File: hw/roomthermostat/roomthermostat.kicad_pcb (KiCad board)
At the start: 2 copper layers, 68 x 68 mm, 15 parts, among them U1 TSIC206_SOIC8

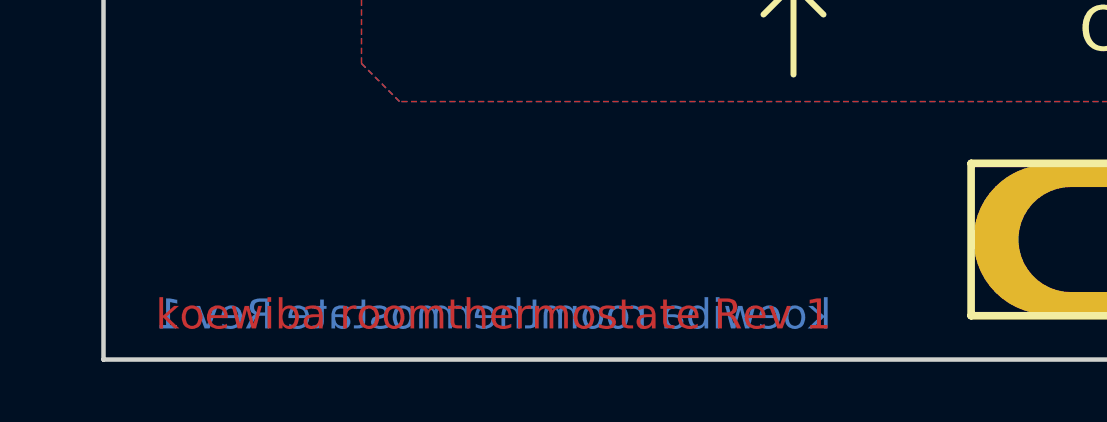
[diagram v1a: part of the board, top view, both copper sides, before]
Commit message: make roomthermostat compatible to bus-module_atmega328 rev A and rev B
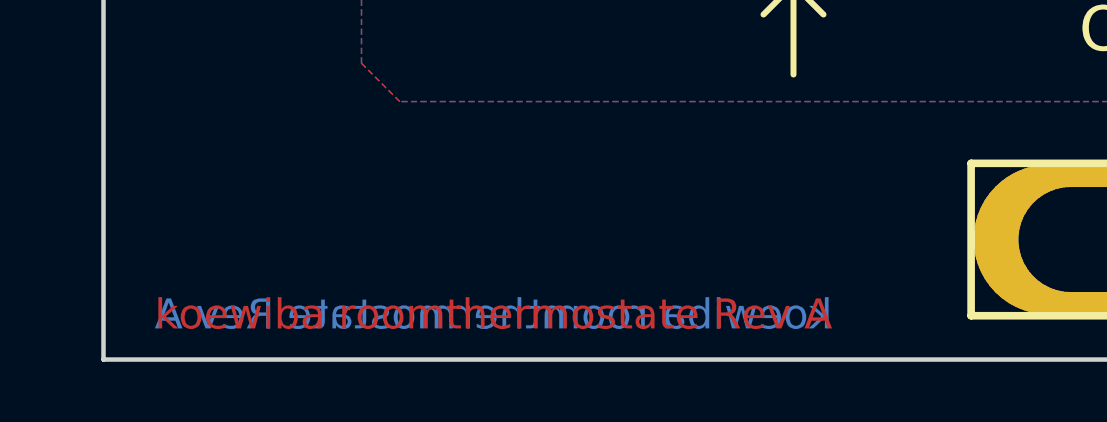
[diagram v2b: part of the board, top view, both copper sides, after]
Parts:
- LOGO1: value Open Hardware -> OPEN_HARDWARE_1
- MOD1: value bus-module_atmega328 -> bus-module_atmega328_revB
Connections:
- MOD1 pad 3: VCC -> (no net)
- MOD1 pad 4: VCC -> (no net)
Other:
- board text added: "koewiba roomthermostate Rev A"
- board text removed: "koewiba roomthermostate Rev 1"
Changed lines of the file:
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@@
   (title_block
     (title roomthermostat)
-    (date 2018-06-14)
-    (rev 1)
+    (date 2018-09-22)
+    (rev A)
     (company koewiba)
   )
@@
       (drillshape 0)
       (scaleselection 1)
-      (outputdirectory "pcb"))
+      (outputdirectory "gerber"))
   )
   (net 0 "")
@@
       (effects (font (size 1 1) (thickness 0.15)) (justify mirror))
     )
-    (fp_text value bus-module_atmega328 (at -12.4 -11.84 90) (layer B.Fab)
+    (fp_text value bus-module_atmega328_revB (at -12.4 -11.84 90) (layer B.Fab)
       (effects (font (size 1 1) (thickness 0.15)) (justify mirror))
     )
@@
     (pad 5 thru_hole circle (at -5.08 0 90) (size 1.8 1.8) (drill 0.9) (layers *.Cu *.Mask B.SilkS)
       (net 11 /KEY1))
-    (pad 4 thru_hole circle (at -2.57 2.54 90) (size 1.8 1.8) (drill 0.9) (layers *.Cu *.Mask B.SilkS)
-      (net 1 VCC))
-    (pad 3 thru_hole circle (at -2.54 0 90) (size 1.8 1.8) (drill 0.9) (layers *.Cu *.Mask B.SilkS)
-      (net 1 VCC))
+    (pad 4 thru_hole circle (at -2.57 2.54 90) (size 1.8 1.8) (drill 0.9) (layers *.Cu *.Mask B.SilkS))
+    (pad 3 thru_hole circle (at -2.54 0 90) (size 1.8 1.8) (drill 0.9) (layers *.Cu *.Mask B.SilkS))
     (pad 2 thru_hole circle (at -0.03 2.54 90) (size 1.8 1.8) (drill 0.9) (layers *.Cu *.Mask B.SilkS)
       (net 2 GND))
@@
       (effects (font (size 1.27 1.27) (thickness 0.254)))
     )
-    (fp_text value "Open Hardware" (at 0.30988 6.56082) (layer F.Fab) hide
+    (fp_text value OPEN_HARDWARE_1 (at 0.30988 6.56082) (layer F.Fab) hide
       (effects (font (size 1.27 1.27) (thickness 0.254)))
     )
@@
     (effects (font (size 1 1) (thickness 0.2)) (justify mirror))
   )
-  (gr_text "koewiba roomthermostate Rev 1" (at 75.915 132.87) (layer B.Cu)
+  (gr_text "koewiba roomthermostate Rev A" (at 75.915 132.87) (layer B.Cu)
     (effects (font (size 1 1) (thickness 0.2)) (justify mirror))
   )
-  (gr_text "koewiba roomthermostate Rev 1" (at 75.915 132.87) (layer F.Cu)
+  (gr_text "koewiba roomthermostate Rev A" (at 75.915 132.87) (layer F.Cu)
     (effects (font (size 1 1) (thickness 0.2)))
   )

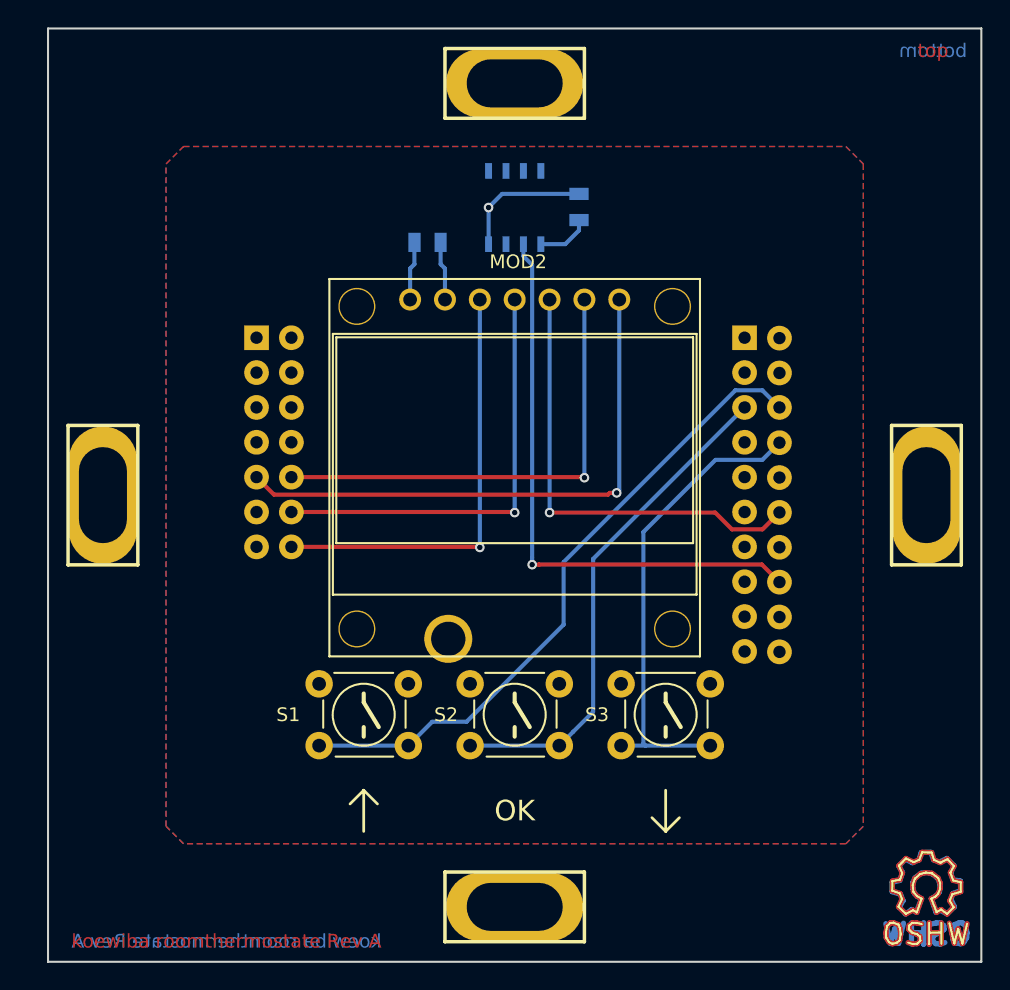
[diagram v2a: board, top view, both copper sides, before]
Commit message: changed pushbuttons of roomthermostate
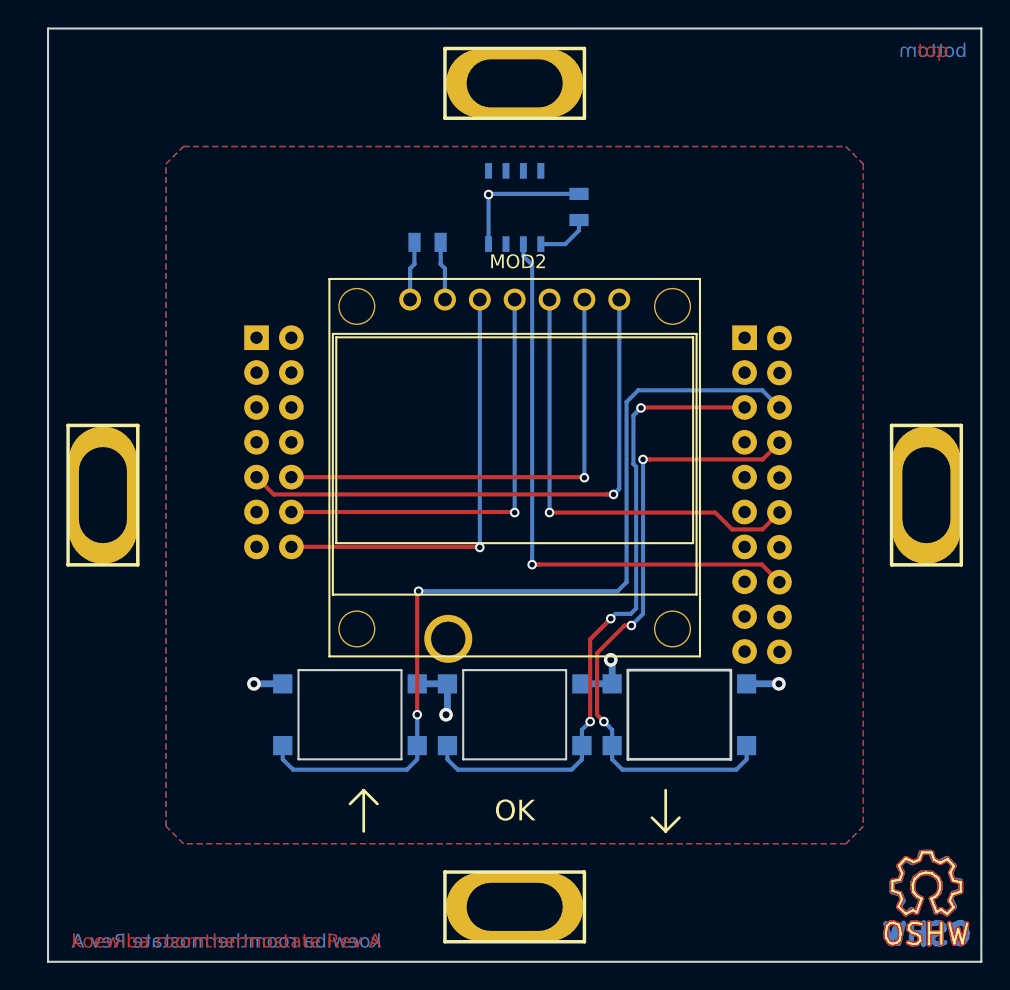
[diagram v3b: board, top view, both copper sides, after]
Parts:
- S1, S2, S3: footprint Switch_Miscelleaneus:PHAP3301 -> Switch_Miscelleaneus:TactileSwitch_SPST_SMD_JTP-1138_BacksideMount; moved to B.Cu
- moved S1 1.00 mm to (84.9, 116.4)
- moved S3 1.00 mm to (108.9, 116.4)
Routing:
- net /KEY0: track 47.5 -> 64.3 mm, vias 0 -> 2
- net GND: track 14.0 -> 27.4 mm, vias 1 -> 5
- net /KEY2: track 34.7 -> 45.8 mm, vias 0 -> 3
- net /KEY1: track 36.7 -> 47.2 mm, vias 0 -> 3
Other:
- outline, holes or cut-outs redrawn
- net class Power added: clearance 0.2, trace_width 0.5, via_dia 1, via_drill 0.5

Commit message: Change pin-assignment of display and temp.sensor
* bumped revision to rev B
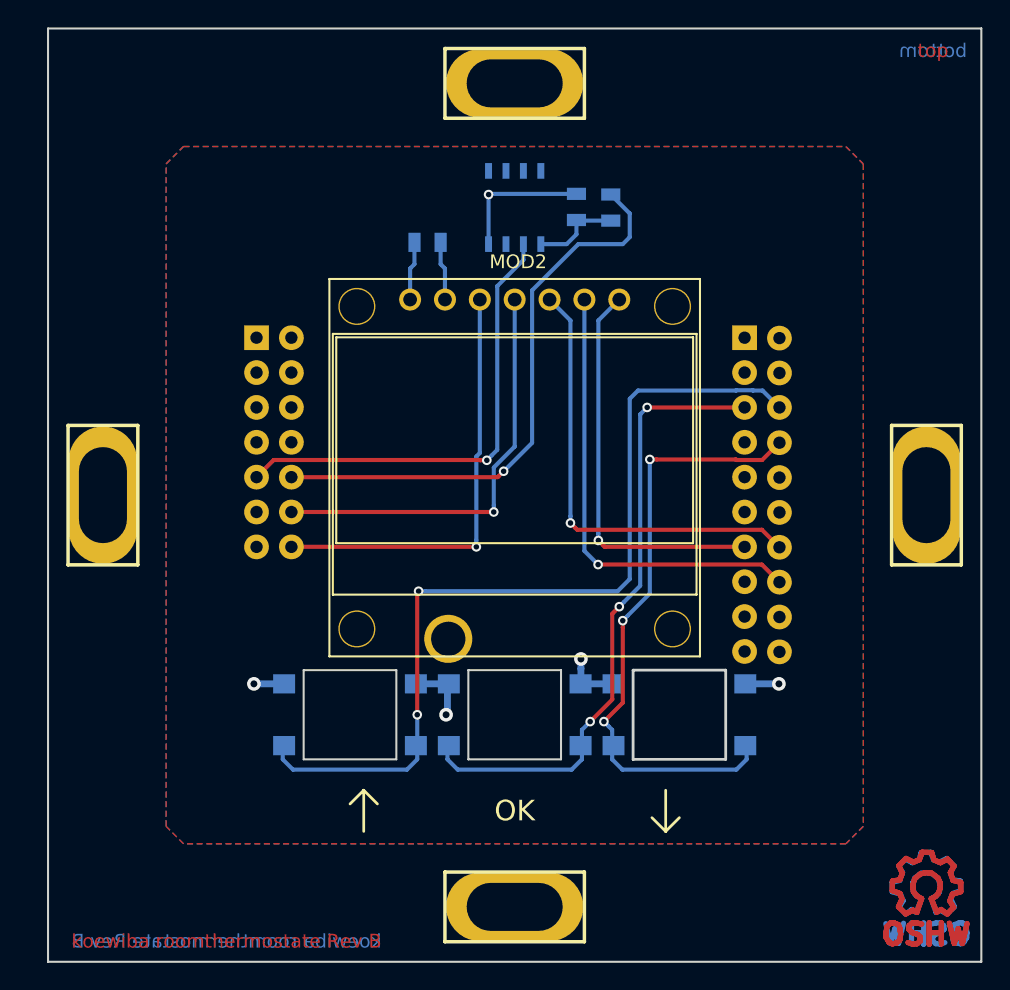
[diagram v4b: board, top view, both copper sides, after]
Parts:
- added R1: 220, Resistor:R_0805, B.Cu at (103.9, 79.4)
- LOGO1: footprint Symbol:Symbol_OSHW-Logo_SilkScreen -> Symbol:Symbol_OSHW-Logo_Copper
- S1, S2, S3: footprint Switch_Miscelleaneus:TactileSwitch_SPST_SMD_JTP-1138_BacksideMount -> Switch_Miscelleaneus:PushButton_SPST_SMD_JTP-1138_BacksideMount
- moved C2 0.19 mm to (101.4, 79.4)
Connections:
- C2 pad 1: VCC -> Net-(C2-Pad1)
- MOD1 pad 10: (no net) -> Net-(MOD1-Pad10)
- MOD1 pad 13: (no net) -> /DISP_CS
- MOD1 pad 14: (no net) -> /DISP_RESET
- MOD1 pad 15: (no net) -> Net-(MOD1-Pad15)
- MOD1 pad 16: /TEMP -> /DISP_A0
- MOD1 pad 18: (no net) -> Net-(MOD1-Pad18)
- MOD1 pad 25: (no net) -> Net-(MOD1-Pad25)
- MOD1 pad 26: (no net) -> Net-(MOD1-Pad26)
- MOD1 pad 27: (no net) -> Net-(MOD1-Pad27)
- MOD1 pad 28: (no net) -> Net-(MOD1-Pad28)
- MOD1 pad 29: //DISP_CS -> /TEMP
- MOD1 pad 3: (no net) -> Net-(MOD1-Pad3)
- MOD1 pad 30: /DISP_A0 -> /TEMP_POW
- MOD1 pad 31: (no net) -> Net-(MOD1-Pad31)
- MOD1 pad 33: (no net) -> Net-(MOD1-Pad33)
- MOD1 pad 4: (no net) -> Net-(MOD1-Pad4)
- MOD1 pad 7: (no net) -> Net-(MOD1-Pad7)
- MOD1 pad 9: (no net) -> Net-(MOD1-Pad9)
- MOD2 pad 5: //RESET -> /DISP_RESET
- MOD2 pad 7: //DISP_CS -> /DISP_CS
- U1 pad 1: VCC -> Net-(C2-Pad1)
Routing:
- net /TEMP_POW: track 0.00 -> 42.1 mm, vias 0 -> 1
- net //DISP_CS: track 40.9 -> 0.00 mm, vias 1 -> 0
- net //RESET: track 33.3 -> 0.00 mm, vias 1 -> 0
- net /DISP_RESET: track 0.00 -> 32.9 mm, vias 0 -> 1
- net /DISP_CS: track 0.00 -> 29.0 mm, vias 0 -> 1
- net /TEMP: track 42.2 -> 34.2 mm
- net Net-(C2-Pad1): track 0.00 -> 6.46 mm
- net VCC: track 8.24 -> 4.30 mm
- net /KEY1: track 47.2 -> 46.1 mm
- net /KEY2: track 45.8 -> 44.9 mm
- net /DISP_MOSI: track 31.8 -> 30.9 mm
- net /DISP_A0: track 34.3 -> 33.5 mm
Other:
- outline, holes or cut-outs redrawn
- rule trace_min: 0.2 -> 0.3
- board text added: "koewiba roomthermostate Rev B"
- board text removed: "koewiba roomthermostate Rev A"

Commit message: Move temperature sensor to other PCB side
* so the temperature senso faces into the room, not into the wall
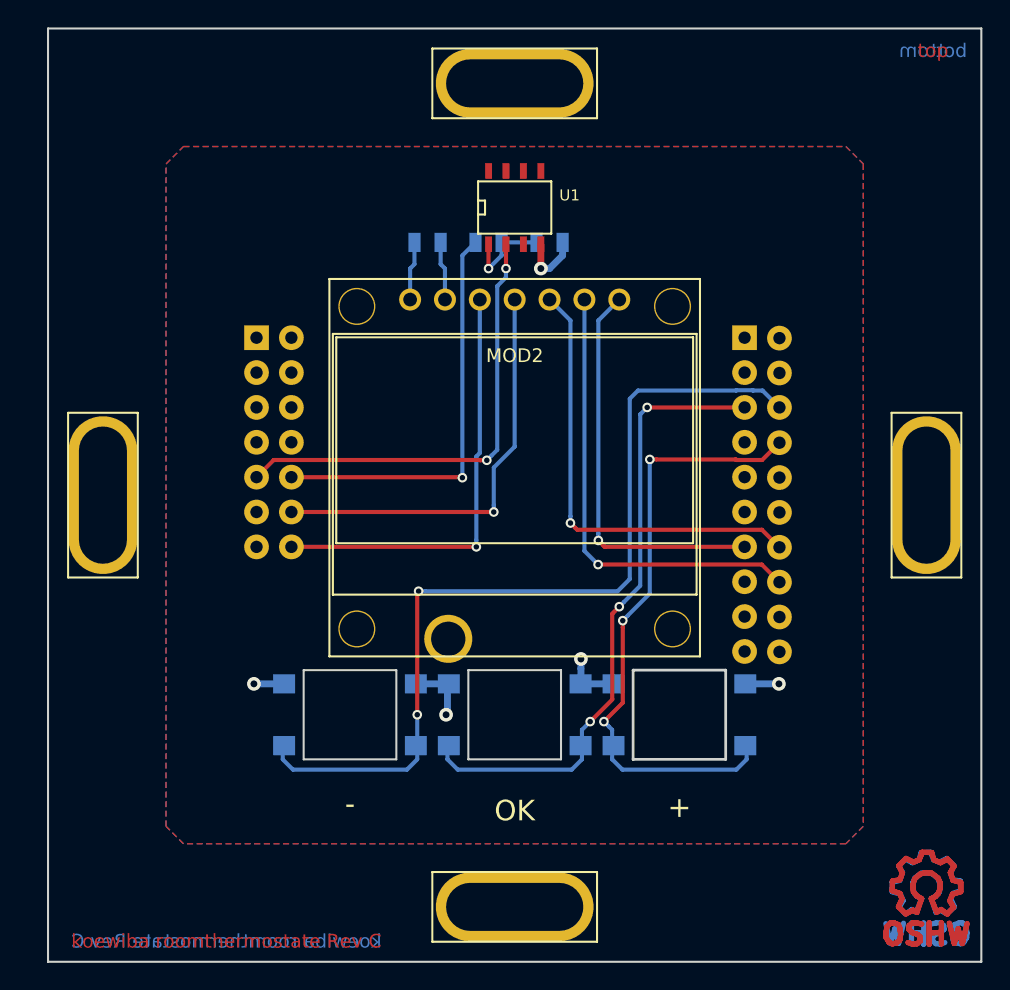
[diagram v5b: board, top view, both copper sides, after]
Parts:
- H1, H2, H3, H4: footprint Mechanical:HOLE_3.5x7mm -> Mechanical:HOLE_3.5x10mm
- U1: moved to F.Cu
- moved R1 9.26 mm to (95.0, 82.0), turned to 180 degrees
- moved C2 3.24 mm to (99.5, 82.0), turned to 0 degrees
- turned U1 to 0 degrees
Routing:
- net /TEMP_POW: track 42.1 -> 30.0 mm
- net GND: track 27.7 -> 22.2 mm
- net /TEMP: track 34.2 -> 33.6 mm, vias 1 -> 2
- net Net-(C2-Pad1): track 6.46 -> 6.62 mm, vias 0 -> 1
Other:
- net class Default removed
- net class Power removed
- board text added: "+"
- board text added: "-"
- board text added: "koewiba roomthermostate Rev C"
- board text removed: "koewiba roomthermostate Rev B"

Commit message: roomthermostat: Update PCB edged and add ext. sensor
* add edge.cuts cutouts for mounting screws and frame
* add external connector for temperature sensor
  (do not add internal and external sensor at the same time!)
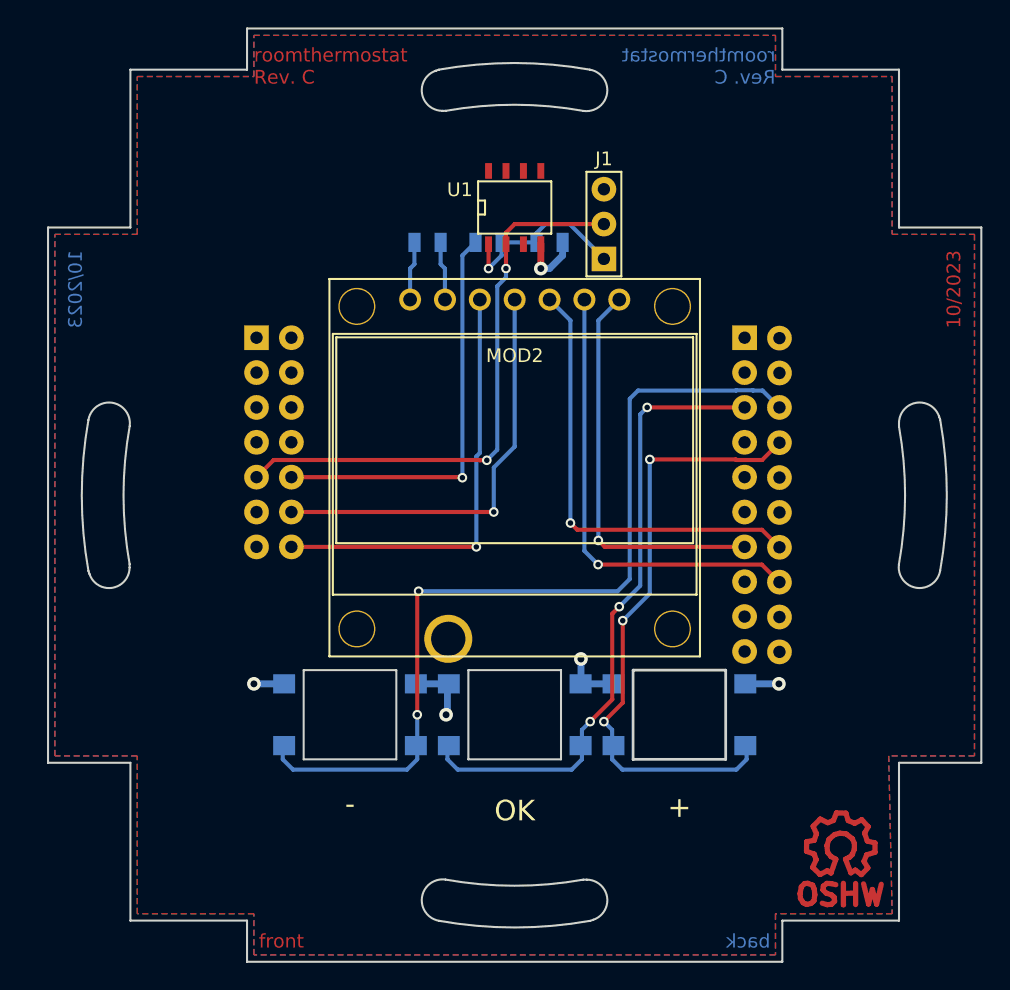
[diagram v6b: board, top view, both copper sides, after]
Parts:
- removed H1, H2, H3, H4: HOLE, Mechanical:HOLE_3.5x10mm
- removed the LOGO1 at (126.9, 128.9) (x3)
- added J1: CONN_3X1, Connector_Header:HEADER_3x1, F.Cu at (103.4, 83.2)
- added LOGO1: OPEN_HARDWARE_1, Symbol:Symbol_OSHW-Logo_Copper, F.Cu at (120.7, 126.0)
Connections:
- net //RESET renamed //RESET
- MOD1 pad 10: Net-(MOD1-Pad10) -> unconnected-(MOD1-Pad10)
- MOD1 pad 15: Net-(MOD1-Pad15) -> unconnected-(MOD1-Pad15)
- MOD1 pad 18: Net-(MOD1-Pad18) -> unconnected-(MOD1-Pad18)
- MOD1 pad 25: Net-(MOD1-Pad25) -> unconnected-(MOD1-Pad25)
- MOD1 pad 26: Net-(MOD1-Pad26) -> unconnected-(MOD1-Pad26)
- MOD1 pad 27: Net-(MOD1-Pad27) -> unconnected-(MOD1-Pad27)
- MOD1 pad 28: Net-(MOD1-Pad28) -> unconnected-(MOD1-Pad28)
- MOD1 pad 3: Net-(MOD1-Pad3) -> unconnected-(MOD1-Pad3)
- MOD1 pad 31: Net-(MOD1-Pad31) -> unconnected-(MOD1-Pad31)
- MOD1 pad 33: Net-(MOD1-Pad33) -> unconnected-(MOD1-Pad33)
- MOD1 pad 4: Net-(MOD1-Pad4) -> unconnected-(MOD1-Pad4)
- MOD1 pad 7: Net-(MOD1-Pad7) -> unconnected-(MOD1-Pad7)
- MOD1 pad 9: Net-(MOD1-Pad9) -> unconnected-(MOD1-Pad9)
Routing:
- net /TEMP: track 33.6 -> 41.9 mm
- net Net-(C2-Pad1): track 6.62 -> 13.6 mm
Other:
- outline, holes or cut-outs redrawn
- board text added: "10/2023"
- board text added: "back"
- board text added: "front"
- board text added: "roomthermostat Rev. C"
- board text removed: "bottom"
- board text removed: "koewiba roomthermostate Rev C"
- board text removed: "top"

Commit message: roomthermostat: move pushbuttons to front side
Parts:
- S1, S2, S3: moved to F.Cu
- turned S1 to 180 degrees
- turned S2 to 180 degrees
- turned S3 to 180 degrees
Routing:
- net GND: track 22.1 -> 9.01 mm, vias 5 -> 1
- net /KEY2: track 44.9 -> 40.7 mm, vias 3 -> 2
- net /KEY0: track 64.3 -> 62.2 mm, vias 2 -> 1
- net /KEY1: vias 3 -> 2
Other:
- outline, holes or cut-outs redrawn
